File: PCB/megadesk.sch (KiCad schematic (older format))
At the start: 20 parts, among them J1 Interface, J2 FFC, J3 AVR-ISP-6, U1 L7812, U2 L7805, U3 ATTINY841-SSU, U4 MCP2003B

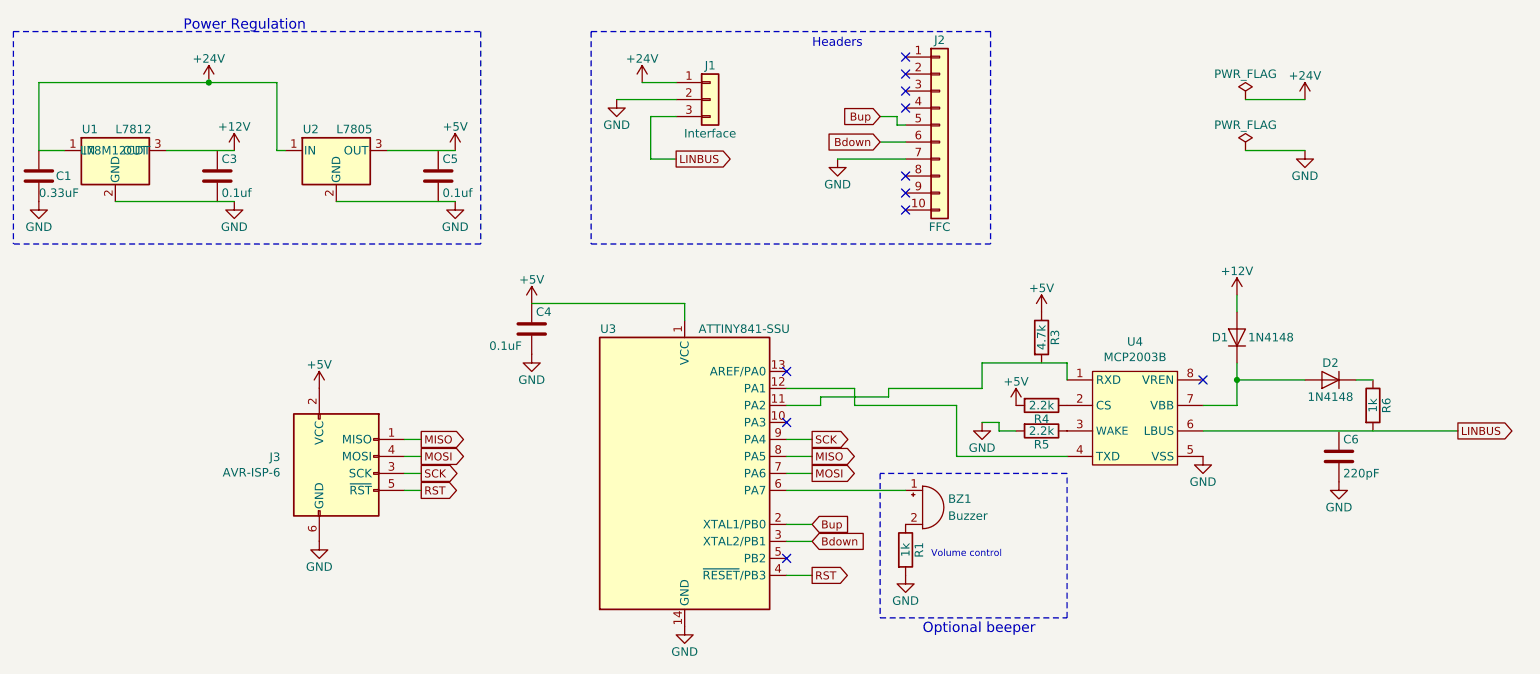
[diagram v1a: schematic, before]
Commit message: simplify resistors and fix programming header
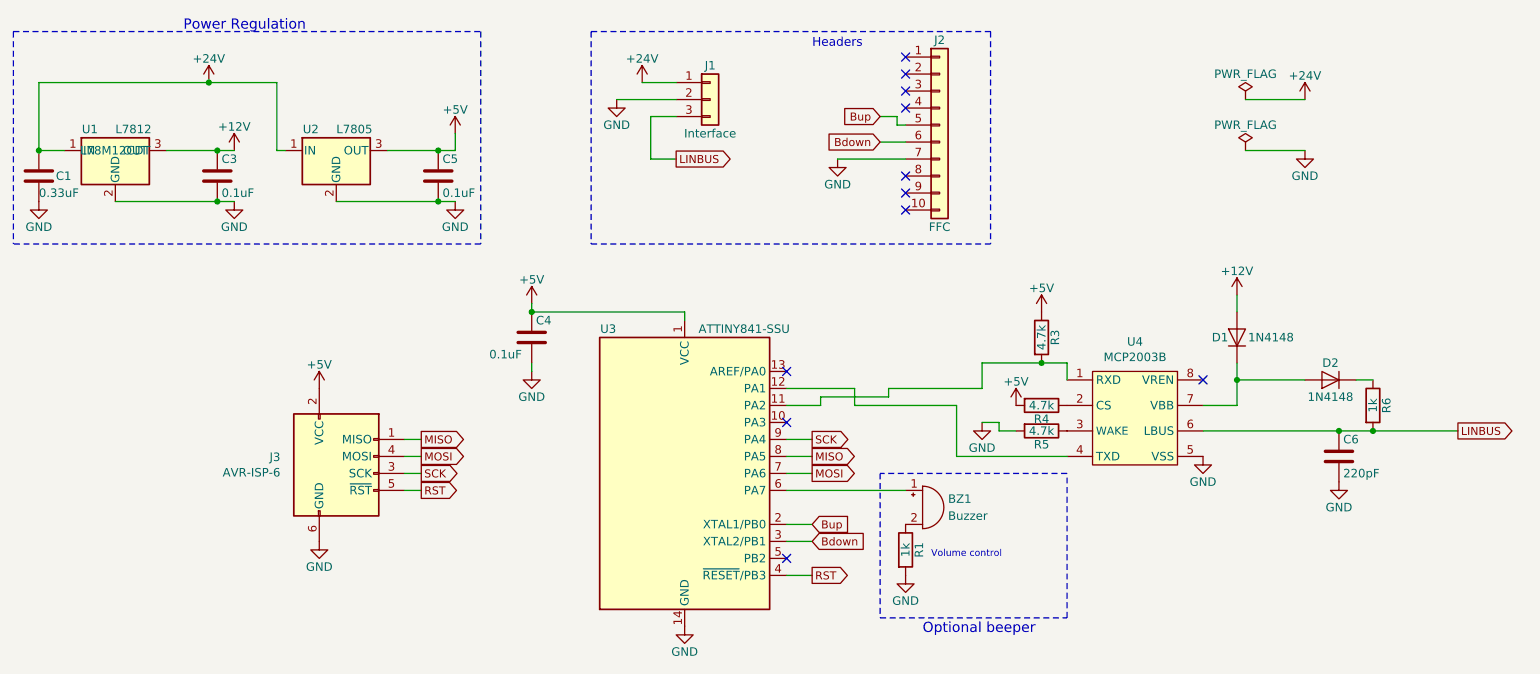
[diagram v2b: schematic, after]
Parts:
- removed U4: MCP2003B, Package_SO:SOIC-8_3.9x4.9mm_P1.27mm, symbol Custom:MCP2003B
- added U4: MCP2003B, Package_SO:SOIC-8_3.9x4.9mm_P1.27mm, symbol !Custom:MCP2003B
- BZ1: footprint Buzzer_Beeper:Buzzer_CUI_CPT-9019S-SMT -> !Greg:Buzzer_Murata_PKMCS0909E4000-R1-HAND-SOLDER; LCSC (none) -> DNP
- C1: LCSC (none) -> C307572
- C3, C5: value 0.1uf -> 0.1uF; LCSC (none) -> C24497
- C4: LCSC (none) -> C24497
- C6: LCSC (none) -> C1854
- D1, D2: LCSC (none) -> C2128
- J1, J2: LCSC (none) -> DNP
- J3: footprint !Custom:AVR-ISP -> Connector_PinHeader_2.54mm:PinHeader_2x03_P2.54mm_Vertical; LCSC (none) -> DNP
- R1, R6: LCSC (none) -> C4410
- R3: LCSC (none) -> C17936
- R4, R5: value 2.2k -> 4.7k; LCSC (none) -> C17936
- U1: LCSC (none) -> C67851
- U2: LCSC (none) -> C20719
- U3: LCSC (none) -> C219103
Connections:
- net +12V: now also C3.1
- net +5V: now also C5.1
- net GND: now also C3.2, C5.2, U4.5 (VSS)
- net LINBUS: now also C6.1, R6.2, U4.6 (LBUS)
- net at R5.1: now also U4.3 (WAKE)
- net at R3.2: now also U3.11 (PA2), U4.1 (RXD)
- net at R4.1: now also U4.2 (CS)
- net at D1.1 (K), D2.2 (A): now also U4.7 (VBB)
- net at U3.12 (PA1): now also U4.4 (TXD)
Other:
- moved on the sheet: C4
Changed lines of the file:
@@
 F 3 "" H 2500 1350 50  0001 C CNN
 F 4 "L78M05CDT" H 2500 1400 50  0001 C CNN "Part Number"
+F 5 "C20719" H 2500 1400 50  0001 C CNN "LCSC"
 	1    2500 1400
 	1    0    0    -1
@@
 L power:+5V #PWR03
 U 1 1 5A824E86
-P 3200 1400
-F 0 "#PWR03" H 3200 1250 50  0001 C CNN
-F 1 "+5V" H 3200 1540 50  0000 C CNN
-F 2 "" H 3200 1400 50  0001 C CNN
-F 3 "" H 3200 1400 50  0001 C CNN
-	1    3200 1400
+P 3200 1300
+F 0 "#PWR03" H 3200 1150 50  0001 C CNN
+F 1 "+5V" H 3200 1440 50  0000 C CNN
+F 2 "" H 3200 1300 50  0001 C CNN
+F 3 "" H 3200 1300 50  0001 C CNN
+	1    3200 1300
 	1    0    0    -1
 $EndComp
@@
 P 3100 1550
 F 0 "C5" H 3125 1650 50  0000 L CNN
-F 1 "0.1uf" H 3125 1450 50  0000 L CNN
+F 1 "0.1uF" H 3125 1450 50  0000 L CNN
 F 2 "Capacitor_SMD:C_1206_3216Metric" H 3138 1400 50  0001 C CNN
 F 3 "" H 3100 1550 50  0001 C CNN
+F 4 "C24497" H 3100 1550 50  0001 C CNN "LCSC"
 	1    3100 1550
 	1    0    0    -1
@@
 P 6650 3050
 F 0 "R5" V 6730 3050 50  0000 C CNN
-F 1 "2.2k" V 6650 3050 50  0000 C CNN
+F 1 "4.7k" V 6650 3050 50  0000 C CNN
 F 2 "Resistor_SMD:R_1206_3216Metric" V 6580 3050 50  0001 C CNN
 F 3 "" H 6650 3050 50  0001 C CNN
+F 4 "C17936" H 6650 3050 50  0001 C CNN "LCSC"
 	1    6650 3050
 	0    1    1    0
@@
 F 2 "Resistor_SMD:R_1206_3216Metric" V 6580 2500 50  0001 C CNN
 F 3 "" H 6650 2500 50  0001 C CNN
+F 4 "C17936" H 6650 2500 50  0001 C CNN "LCSC"
 	1    6650 2500
 	1    0    0    -1
@@
 P 6650 2900
 F 0 "R4" V 6730 2900 50  0000 C CNN
-F 1 "2.2k" V 6650 2900 50  0000 C CNN
+F 1 "4.7k" V 6650 2900 50  0000 C CNN
 F 2 "Resistor_SMD:R_1206_3216Metric" V 6580 2900 50  0001 C CNN
 F 3 "" H 6650 2900 50  0001 C CNN
+F 4 "C17936" H 6650 2900 50  0001 C CNN "LCSC"
 	1    6650 2900
 	0    1    1    0
@@
 F 4 "L78M12CDT" H 1200 1400 50  0000 C CNN "Part Number"
 F 5 "STMicroelectronics L78M12CDT" H 1200 1400 60  0001 C CNN "Details"
+F 6 "C67851" H 1200 1400 50  0001 C CNN "LCSC"
 	1    1200 1400
 	1    0    0    -1
@@
 P 1800 1550
 F 0 "C3" H 1825 1650 50  0000 L CNN
-F 1 "0.1uf" H 1825 1450 50  0000 L CNN
+F 1 "0.1uF" H 1825 1450 50  0000 L CNN
 F 2 "Capacitor_SMD:C_1206_3216Metric" H 1838 1400 50  0001 C CNN
 F 3 "" H 1800 1550 50  0001 C CNN
+F 4 "C24497" H 1800 1550 50  0001 C CNN "LCSC"
 	1    1800 1550
 	1    0    0    -1
@@
 F 2 "Resistor_SMD:R_1206_3216Metric" V 8530 2900 50  0001 C CNN
 F 3 "" H 8600 2900 50  0001 C CNN
+F 4 "C4410" H 8600 2900 50  0001 C CNN "LCSC"
 	1    8600 2900
 	1    0    0    -1
@@
 F 2 "Capacitor_SMD:C_1206_3216Metric" H 8438 3050 50  0001 C CNN
 F 3 "" H 8400 3200 50  0001 C CNN
+F 4 "C1854" H 8400 3200 50  0001 C CNN "LCSC"
 	1    8400 3200
 	1    0    0    -1
@@
 F 2 "Pin_Headers:Pin_Header_Angled_1x03_Pitch2.54mm" H 4700 1100 50  0001 C CNN
 F 3 "" H 4700 1100 50  0001 C CNN
+F 4 "DNP" H 4700 1100 50  0001 C CNN "LCSC"
 	1    4700 1100
 	1    0    0    -1
@@
 F 2 "Diodes_SMD:D_SOD-323_HandSoldering" H 7800 2500 50  0001 C CNN
 F 3 "" H 7800 2500 50  0001 C CNN
+F 4 "C2128" H 7800 2500 50  0001 C CNN "LCSC"
 	1    7800 2500
 	0    -1   -1   0
@@
 F 2 "Diodes_SMD:D_SOD-323_HandSoldering" H 8350 2750 50  0001 C CNN
 F 3 "" H 8350 2750 50  0001 C CNN
+F 4 "C2128" H 8350 2750 50  0001 C CNN "LCSC"
 	1    8350 2750
 	-1   0    0    1
@@
 F 2 "Capacitor_SMD:C_1206_3216Metric" H 788 1400 50  0001 C CNN
 F 3 "" H 750 1550 50  0001 C CNN
+F 4 "C307572" H 750 1550 50  0001 C CNN "LCSC"
 	1    750  1550
 	1    0    0    -1
@@
 F 3 "" H 4550 3300 50  0001 C CNN
 F 4 "ATTINY841-SSU" H 4550 3300 50  0001 C CNN "Part Number"
+F 5 "C219103" H 4550 3300 50  0001 C CNN "LCSC"
 	1    4550 3300
 	1    0    0    -1
@@
 L Device:C C4
 U 1 1 5AA1F9DA
-P 3650 2450
-F 0 "C4" H 3675 2550 50  0000 L CNN
-F 1 "0.1uF" H 3400 2350 50  0000 L CNN
-F 2 "Capacitor_SMD:C_1206_3216Metric" H 3688 2300 50  0001 C CNN
-F 3 "" H 3650 2450 50  0001 C CNN
-	1    3650 2450
+P 3650 2500
+F 0 "C4" H 3675 2600 50  0000 L CNN
+F 1 "0.1uF" H 3400 2400 50  0000 L CNN
+F 2 "Capacitor_SMD:C_1206_3216Metric" H 3688 2350 50  0001 C CNN
+F 3 "" H 3650 2500 50  0001 C CNN
+F 4 "C24497" H 3650 2500 50  0001 C CNN "LCSC"
+	1    3650 2500
 	1    0    0    -1
 $EndComp
@@
 L power:GND #PWR020
 U 1 1 5AA1FA9D
-P 3650 2600
-F 0 "#PWR020" H 3650 2350 50  0001 C CNN
-F 1 "GND" H 3650 2450 50  0000 C CNN
-F 2 "" H 3650 2600 50  0001 C CNN
-F 3 "" H 3650 2600 50  0001 C CNN
-	1    3650 2600
+P 3650 2700
+F 0 "#PWR020" H 3650 2450 50  0001 C CNN
+F 1 "GND" H 3650 2550 50  0000 C CNN
+F 2 "" H 3650 2700 50  0001 C CNN
+F 3 "" H 3650 2700 50  0001 C CNN
+	1    3650 2700
 	1    0    0    -1
 $EndComp
@@
 F 3 "" H 6050 1250 50  0001 C CNN
 F 4 "1-84981-0" H 6050 1250 50  0001 C CNN "Part Number"
+F 5 "DNP" H 6050 1250 50  0001 C CNN "LCSC"
 	1    6050 1250
 	1    0    0    -1
@@
 F 0 "BZ1" H 6100 3550 50  0000 L CNN
 F 1 "Buzzer" H 6100 3450 50  0000 L CNN
-F 2 "Buzzer_Beeper:Buzzer_CUI_CPT-9019S-SMT" V 5925 3600 50  0001 C CNN
+F 2 "!Greg:Buzzer_Murata_PKMCS0909E4000-R1-HAND-SOLDER" V 5925 3600 50  0001 C CNN
 F 3 "" V 5925 3600 50  0001 C CNN
 F 4 "CPT-9019S-SM" H 5950 3500 50  0001 C CNN "Part Number"
+F 5 "DNP" H 5950 3500 50  0001 C CNN "LCSC"
 	1    5950 3500
 	1    0    0    -1
@@
 F 2 "Resistor_SMD:R_1206_3216Metric" V 5780 3750 50  0001 C CNN
 F 3 "" H 5850 3750 50  0001 C CNN
+F 4 "C4410" H 5850 3750 50  0001 C CNN "LCSC"
 	1    5850 3750
 	1    0    0    -1
@@
 	7800 2750 7800 2650
 Wire Wire Line
-	4550 2400 4550 2300
-Wire Wire Line
-	4550 2300 3650 2300
+	4550 2400 4550 2350
 Wire Wire Line
 	2150 1000 2150 1400
@@
 F 0 "J3" H 2171 3396 50  0000 R CNN
 F 1 "AVR-ISP-6" H 2171 3305 50  0000 R CNN
-F 2 "!Custom:AVR-ISP" V 2250 3350 50  0001 C CNN
+F 2 "Connector_PinHeader_2.54mm:PinHeader_2x03_P2.54mm_Vertical" V 2250 3350 50  0001 C CNN
 F 3 " ~" H 1225 2750 50  0001 C CNN
+F 4 "DNP" H 2500 3300 50  0001 C CNN "LCSC"
 	1    2500 3300
 	1    0    0    -1
@@
 Wire Wire Line
 	3000 3100 2900 3100
-$Comp
-L Custom:MCP2003B U4
-U 1 1 5EA90AFC
+Wire Wire Line
+	1200 1700 1800 1700
+Wire Wire Line
+	1500 1400 1800 1400
+Wire Wire Line
+	6300 2650 6650 2650
+Wire Wire Line
+	7600 3050 8400 3050
+Wire Notes Line
+	4000 700  4000 1950
+Wire Notes Line
+	4000 700  6350 700
+Wire Notes Line
+	4000 1950 6350 1950
+Wire Notes Line
+	6350 700  6350 1950
+$Comp
+L !Custom:MCP2003B U4
+U 1 1 5EF811C0
 P 7200 2950
 F 0 "U4" H 7200 3375 50  0000 C CNN
@@
 F 2 "Package_SO:SOIC-8_3.9x4.9mm_P1.27mm" H 7200 2500 50  0001 C CNN
 F 3 "http://ww1.microchip.com/downloads/en/DeviceDoc/22299B.pdf" H 7300 2950 50  0001 C CNN
+F 4 "C152207" H 7200 2950 50  0001 C CNN "LCSC"
 	1    7200 2950
 	1    0    0    -1
 $EndComp
 Wire Wire Line
-	2800 1400 3200 1400
-Wire Wire Line
-	2500 1700 3200 1700
-Wire Wire Line
-	1200 1700 1900 1700
-Wire Wire Line
-	1500 1400 1900 1400
-Wire Wire Line
-	6300 2650 6800 2650
-Wire Wire Line
-	7600 3050 9100 3050
-Wire Notes Line
-	4000 700  4000 1950
-Wire Notes Line
-	4000 700  6350 700
-Wire Notes Line
-	4000 1950 6350 1950
-Wire Notes Line
-	6350 700  6350 1950
+	3650 2300 3650 2350
+Wire Wire Line
+	3650 2350 4550 2350
+Connection ~ 3650 2350
+Wire Wire Line
+	3650 2650 3650 2700
+Wire Wire Line
+	2800 1400 3100 1400
+Wire Wire Line
+	3100 1400 3200 1400
+Wire Wire Line
+	3200 1400 3200 1300
+Connection ~ 3100 1400
+Wire Wire Line
+	3200 1700 3100 1700
+Wire Wire Line
+	3100 1700 2500 1700
+Connection ~ 3100 1700
+Connection ~ 1800 1400
+Wire Wire Line
+	1800 1400 1900 1400
+Connection ~ 1800 1700
+Wire Wire Line
+	1800 1700 1900 1700
+Connection ~ 750  1400
+Connection ~ 6650 2650
+Wire Wire Line
+	6650 2650 6800 2650
+Connection ~ 8600 3050
+Wire Wire Line
+	8600 3050 9100 3050
+Connection ~ 8400 3050
+Wire Wire Line
+	8400 3050 8600 3050
 $EndSCHEMATC

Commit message: disassembly video
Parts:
- removed U3: ATTINY841-SSU, Package_SO:SOIC-14_3.9x8.7mm_P1.27mm, symbol MCU_Microchip_ATtiny:ATtiny841-SSU
- added U3: ATtiny841-SS, Package_SO:SOIC-14_3.9x8.7mm_P1.27mm, symbol MCU_Microchip_ATtiny:ATtiny841-SS
- BZ1: Notes (none) -> Substition OK; Part Number CPT-9019S-SM -> PKMCS0909E4000-R1
- C1, C3, C4, C5, C6: Details (none) -> +/- 20% or better
- D1, D2: Notes (none) -> Substitution OK; Part Number (none) -> 1N4148
- J1: Notes (none) -> Substitution OK; Part Number (none) -> Molex 0022288030
- J2: Notes (none) -> Substitution OK; Part Number 1-84981-0 -> TE Connectivity AMP 1-84981-0
- J3: Part Number (none) -> DNP
- R1, R3, R4, R5, R6: Details (none) -> +/- 10% or better
- U1: Details STMicroelectronics L78M12CDT -> (none); Notes (none) -> 35V INPUT; Part Number L78M12CDT -> MC78M12CDTRKG
- U2: LCSC C20719 -> C58069; Notes (none) -> 35V INPUT; Part Number L78M05CDT -> L78M05ABDT-TR
- U4: Part Number (none) -> MCP2003B
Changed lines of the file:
@@
 F 2 "Package_TO_SOT_SMD:TO-252-3_TabPin2" H 2525 1250 50  0001 L CIN
 F 3 "" H 2500 1350 50  0001 C CNN
-F 4 "L78M05CDT" H 2500 1400 50  0001 C CNN "Part Number"
-F 5 "C20719" H 2500 1400 50  0001 C CNN "LCSC"
+F 4 "L78M05ABDT-TR" H 2500 1400 50  0001 C CNN "Part Number"
+F 5 "C58069" H 2500 1400 50  0001 C CNN "LCSC"
+F 6 "35V INPUT" H 2500 1400 50  0001 C CNN "Notes"
 	1    2500 1400
 	1    0    0    -1
@@
 F 3 "" H 3100 1550 50  0001 C CNN
 F 4 "C24497" H 3100 1550 50  0001 C CNN "LCSC"
+F 5 "+/- 20% or better" H 3100 1550 50  0001 C CNN "Details"
 	1    3100 1550
 	1    0    0    -1
@@
 F 3 "" H 6650 3050 50  0001 C CNN
 F 4 "C17936" H 6650 3050 50  0001 C CNN "LCSC"
+F 5 "+/- 10% or better" H 6650 3050 50  0001 C CNN "Details"
 	1    6650 3050
 	0    1    1    0
@@
 F 3 "" H 6650 2500 50  0001 C CNN
 F 4 "C17936" H 6650 2500 50  0001 C CNN "LCSC"
+F 5 "+/- 10% or better" H 6650 2500 50  0001 C CNN "Details"
 	1    6650 2500
 	1    0    0    -1
@@
 F 3 "" H 6650 2900 50  0001 C CNN
 F 4 "C17936" H 6650 2900 50  0001 C CNN "LCSC"
+F 5 "+/- 10% or better" H 6650 2900 50  0001 C CNN "Details"
 	1    6650 2900
 	0    1    1    0
@@
 F 2 "Package_TO_SOT_SMD:TO-252-3_TabPin2" H 1225 1250 50  0001 L CIN
 F 3 "" H 1200 1350 50  0001 C CNN
-F 4 "L78M12CDT" H 1200 1400 50  0000 C CNN "Part Number"
-F 5 "STMicroelectronics L78M12CDT" H 1200 1400 60  0001 C CNN "Details"
+F 4 "MC78M12CDTRKG" H 1200 1400 50  0000 C CNN "Part Number"
+F 5 "" H 1200 1400 60  0001 C CNN "Details"
 F 6 "C67851" H 1200 1400 50  0001 C CNN "LCSC"
+F 7 "35V INPUT" H 1200 1400 50  0001 C CNN "Notes"
 	1    1200 1400
 	1    0    0    -1
@@
 F 3 "" H 1800 1550 50  0001 C CNN
 F 4 "C24497" H 1800 1550 50  0001 C CNN "LCSC"
+F 5 "+/- 20% or better" H 1800 1550 50  0001 C CNN "Details"
 	1    1800 1550
 	1    0    0    -1
@@
 F 3 "" H 8600 2900 50  0001 C CNN
 F 4 "C4410" H 8600 2900 50  0001 C CNN "LCSC"
+F 5 "+/- 10% or better" H 8600 2900 50  0001 C CNN "Details"
 	1    8600 2900
 	1    0    0    -1
@@
 F 3 "" H 8400 3200 50  0001 C CNN
 F 4 "C1854" H 8400 3200 50  0001 C CNN "LCSC"
+F 5 "+/- 20% or better" H 8400 3200 50  0001 C CNN "Details"
 	1    8400 3200
 	1    0    0    -1
@@
 F 3 "" H 4700 1100 50  0001 C CNN
 F 4 "DNP" H 4700 1100 50  0001 C CNN "LCSC"
+F 5 "Molex 0022288030" H 4700 1100 50  0001 C CNN "Part Number"
+F 6 "Substitution OK" H 4700 1100 50  0001 C CNN "Notes"
 	1    4700 1100
 	1    0    0    -1
@@
 F 3 "" H 7800 2500 50  0001 C CNN
 F 4 "C2128" H 7800 2500 50  0001 C CNN "LCSC"
+F 5 "1N4148" H 7800 2500 50  0001 C CNN "Part Number"
+F 6 "Substitution OK" H 7800 2500 50  0001 C CNN "Notes"
 	1    7800 2500
 	0    -1   -1   0
@@
 F 3 "" H 8350 2750 50  0001 C CNN
 F 4 "C2128" H 8350 2750 50  0001 C CNN "LCSC"
+F 5 "1N4148" H 8350 2750 50  0001 C CNN "Part Number"
+F 6 "Substitution OK" H 8350 2750 50  0001 C CNN "Notes"
 	1    8350 2750
 	-1   0    0    1
@@
 F 3 "" H 750 1550 50  0001 C CNN
 F 4 "C307572" H 750 1550 50  0001 C CNN "LCSC"
+F 5 "+/- 20% or better" H 750 1550 50  0001 C CNN "Details"
 	1    750  1550
 	1    0    0    -1
@@
 $EndComp
 $Comp
-L MCU_Microchip_ATtiny:ATtiny841-SSU U3
-U 1 1 5AA1C491
-P 4550 3300
-F 0 "U3" H 4100 4150 50  0000 C CNN
-F 1 "ATTINY841-SSU" H 4900 4150 50  0000 C CNN
-F 2 "Package_SO:SOIC-14_3.9x8.7mm_P1.27mm" H 4550 3100 50  0001 C CIN
-F 3 "" H 4550 3300 50  0001 C CNN
-F 4 "ATTINY841-SSU" H 4550 3300 50  0001 C CNN "Part Number"
-F 5 "C219103" H 4550 3300 50  0001 C CNN "LCSC"
-	1    4550 3300
-	1    0    0    -1
-$EndComp
-$Comp
 L power:GND #PWR019
 U 1 1 5AA1DE4D
@@
 F 3 "" H 3650 2500 50  0001 C CNN
 F 4 "C24497" H 3650 2500 50  0001 C CNN "LCSC"
+F 5 "+/- 20% or better" H 3650 2500 50  0001 C CNN "Details"
 	1    3650 2500
 	1    0    0    -1
@@
 F 2 "!Custom:FFC_10" H 6050 1250 50  0001 C CNN
 F 3 "" H 6050 1250 50  0001 C CNN
-F 4 "1-84981-0" H 6050 1250 50  0001 C CNN "Part Number"
+F 4 "TE Connectivity AMP 1-84981-0" H 6050 1250 50  0001 C CNN "Part Number"
 F 5 "DNP" H 6050 1250 50  0001 C CNN "LCSC"
+F 6 "Substitution OK" H 6050 1250 50  0001 C CNN "Notes"
 	1    6050 1250
 	1    0    0    -1
@@
 F 2 "!Greg:Buzzer_Murata_PKMCS0909E4000-R1-HAND-SOLDER" V 5925 3600 50  0001 C CNN
 F 3 "" V 5925 3600 50  0001 C CNN
-F 4 "CPT-9019S-SM" H 5950 3500 50  0001 C CNN "Part Number"
+F 4 "PKMCS0909E4000-R1" H 5950 3500 50  0001 C CNN "Part Number"
 F 5 "DNP" H 5950 3500 50  0001 C CNN "LCSC"
+F 6 "Substition OK" H 5950 3500 50  0001 C CNN "Notes"
 	1    5950 3500
 	1    0    0    -1
@@
 F 3 "" H 5850 3750 50  0001 C CNN
 F 4 "C4410" H 5850 3750 50  0001 C CNN "LCSC"
+F 5 "+/- 10% or better" H 5850 3750 50  0001 C CNN "Details"
 	1    5850 3750
 	1    0    0    -1
@@
 F 3 " ~" H 1225 2750 50  0001 C CNN
 F 4 "DNP" H 2500 3300 50  0001 C CNN "LCSC"
+F 5 "DNP" H 2500 3300 50  0001 C CNN "Part Number"
 	1    2500 3300
 	1    0    0    -1
@@
 F 1 "MCP2003B" H 7200 3284 50  0000 C CNN
 F 2 "Package_SO:SOIC-8_3.9x4.9mm_P1.27mm" H 7200 2500 50  0001 C CNN
-F 3 "http://ww1.microchip.com/downloads/en/DeviceDoc/22299B.pdf" H 7300 2950 50  0001 C CNN
+F 3 "" H 7300 2950 50  0001 C CNN
 F 4 "C152207" H 7200 2950 50  0001 C CNN "LCSC"
+F 5 "MCP2003B" H 7200 2950 50  0001 C CNN "Part Number"
 	1    7200 2950
 	1    0    0    -1
@@
 Wire Wire Line
 	8400 3050 8600 3050
+$Comp
+L MCU_Microchip_ATtiny:ATtiny841-SS U3
+U 1 1 5F8D16D9
+P 4550 3300
+F 0 "U3" H 4021 3346 50  0000 R CNN
+F 1 "ATtiny841-SS" H 4021 3255 50  0000 R CNN
+F 2 "Package_SO:SOIC-14_3.9x8.7mm_P1.27mm" H 4550 3300 50  0001 C CIN
+F 3 "http://ww1.microchip.com/downloads/en/DeviceDoc/Atmel-8495-8-bit-AVR-Microcontrollers-ATtiny441-ATtiny841_Datasheet.pdf" H 4550 3300 50  0001 C CNN
+	1    4550 3300
+	1    0    0    -1
+$EndComp
 $EndSCHEMATC
